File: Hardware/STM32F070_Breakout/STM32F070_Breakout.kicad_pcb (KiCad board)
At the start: 2 copper layers, 17.8 x 38.1 mm, 34 parts, among them J1 USB_B_Micro, J2 Conn_01x15, J3 Conn_01x15, J4 Conn_01x05, SW1 SW_Push, SW2 SW_Push, U1 AP2112K-3.3, U2 STM32F070CBT6, Y1 32.768kHZ, Y2 16MHz

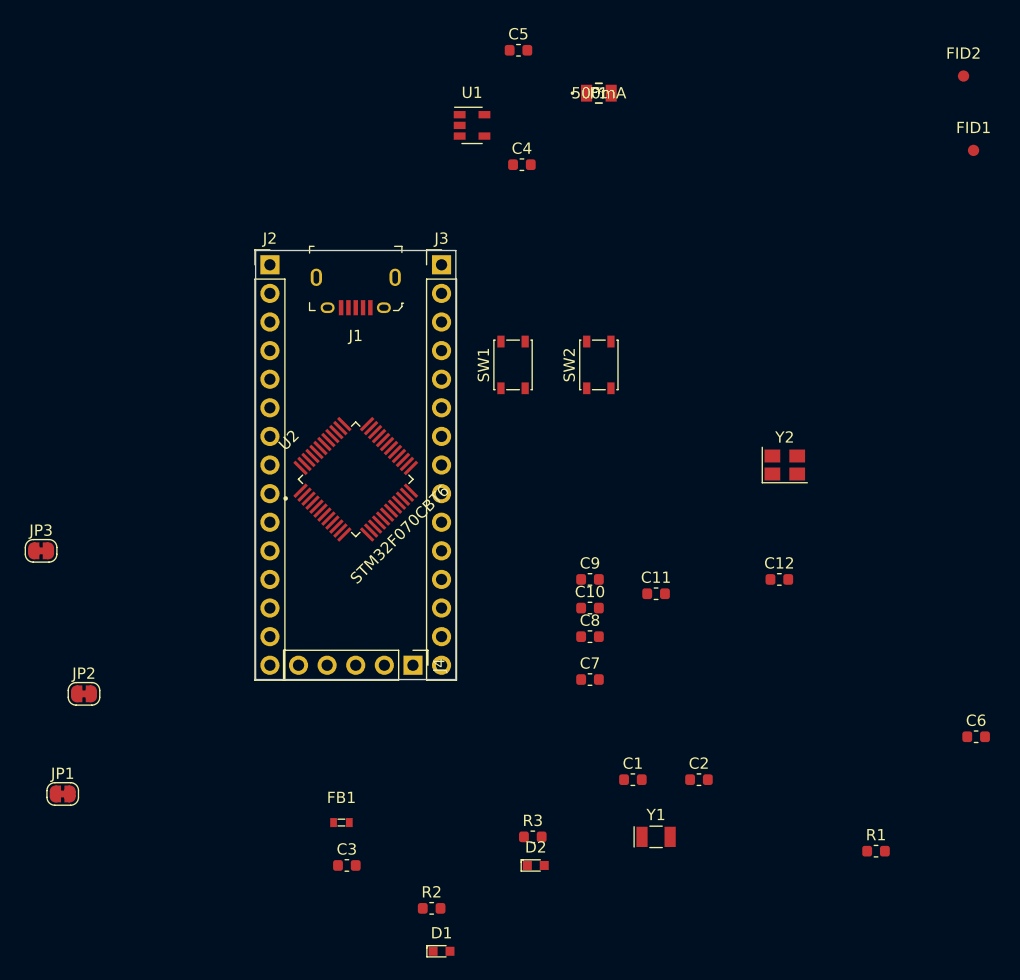
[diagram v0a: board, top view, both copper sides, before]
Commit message: Moved components around. Created BOM.
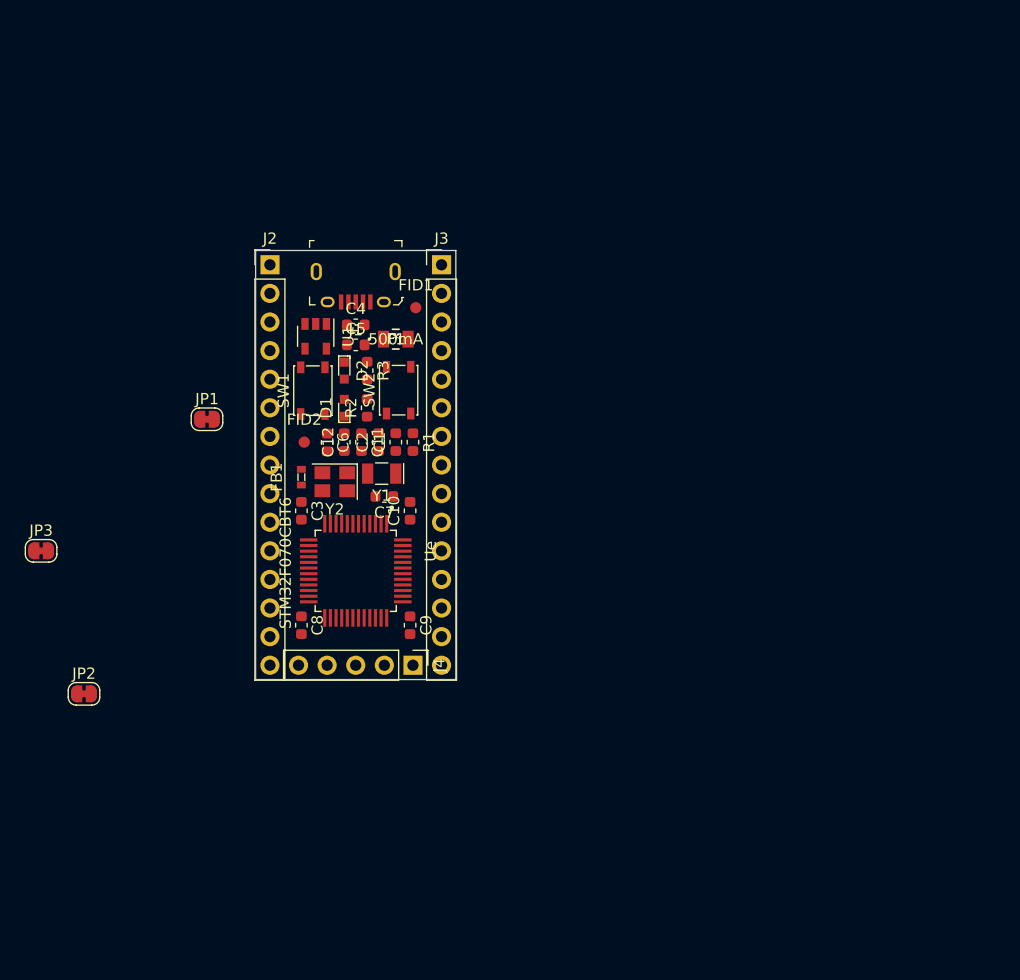
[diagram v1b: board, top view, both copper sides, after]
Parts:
- removed U2: STM32F070CBT6, STM32F070CBT6:QFP50P900X900X160-48N
- added Ue: STM32F070CBT6, STM32F070CBT6:QFP50P900X900X160-48N, F.Cu at (135.9, 104.6)
- moved FID2 67.0 mm to (131.3, 93.2)
- moved C6 63.3 mm to (133.3, 93.2), turned to 270 degrees
- moved R1 54.9 mm to (141.0, 93.2), turned to 270 degrees
- moved FID1 51.5 mm to (141.2, 81.3)
- moved D1 49.0 mm to (134.9, 90.2), turned to 90 degrees
- moved D2 47.1 mm to (134.9, 86.9), turned to 270 degrees
- moved R2 44.8 mm to (136.9, 90.2), turned to 90 degrees
- moved R3 43.9 mm to (136.9, 86.9), turned to 270 degrees
- moved C2 41.3 mm to (137.9, 93.2), turned to 90 degrees
- moved C12 40.5 mm to (134.9, 93.2), turned to 90 degrees
- moved Y1 40.4 mm to (138.2, 96.0), turned to 180 degrees
- moved Y2 40.0 mm to (134.0, 96.7), turned to 180 degrees
- moved C1 36.6 mm to (139.4, 93.2), turned to 90 degrees
- moved JP1 35.7 mm to (122.7, 91.2)
- moved C3 31.8 mm to (131.1, 99.3), turned to 270 degrees
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
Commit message: Components placed
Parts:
- removed Ue: STM32F070CBT6, STM32F070CBT6:QFP50P900X900X160-48N
- added U2: STM32F070CBT6, STM32F070CBT6:QFP50P900X900X160-48N, F.Cu at (135.9, 93.7)
- J2, J3: value Conn_01x15 -> Conn_01x16; footprint Connector_PinHeader_2.54mm:PinHeader_1x15_P2.54mm_Vertical -> Connector_PinHeader_2.54mm:PinHeader_1x16_P2.54mm_Vertical
- JP3: moved to B.Cu
- moved JP2 39.8 mm to (148.0, 98.9), turned to 270 degrees
- moved JP3 35.7 mm to (139.8, 86.9)
- moved JP1 31.4 mm to (149.7, 107.1), turned to 270 degrees
- moved SW2 23.2 mm to (132.1, 110.5)
- moved SW1 23.1 mm to (139.7, 110.5)
- moved C8 22.7 mm to (140.7, 88.9), turned to 90 degrees
- moved C9 22.7 mm to (131.1, 88.9), turned to 90 degrees
- moved D1 21.1 mm to (135.9, 111.3), turned to 0 degrees
- moved R2 19.6 mm to (135.9, 109.7), turned to 0 degrees
- moved R1 16.3 mm to (130.8, 105.9), turned to 90 degrees
- moved FID2 15.6 mm to (140.5, 105.9), turned to 180 degrees
- moved C1 14.6 mm to (132.3, 105.9), turned to 270 degrees
- moved C6 13.6 mm to (138.4, 105.9), turned to 90 degrees
- moved C2 13.3 mm to (133.9, 105.9), turned to 270 degrees
- moved C12 12.9 mm to (136.9, 105.9)
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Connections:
- J1 pad 2: USB_DM -> USB_D-
- J1 pad 3: USB_DP -> USB_D+
- J2 pad 1: AREF -> GND
- J2 pad 10: A6 -> D10
- J2 pad 11: A7 -> D11
- J2 pad 12: A8 -> D13
- J2 pad 13: A9 -> D14
- J2 pad 14: D0 -> D15
- J2 pad 15: D1 -> D16
- J2 pad 2: AGND -> D0
- J2 pad 3: RESET -> D1
- J2 pad 4: A0 -> D2
- J2 pad 5: A1 -> D3
- J2 pad 6: A2 -> D4
- J2 pad 7: A3 -> D5
- J2 pad 8: A4 -> D6
- J2 pad 9: A5 -> D7
- J3 pad 10: D7 -> A4
- J3 pad 11: D6 -> A3
- J3 pad 12: D5 -> A2
- J3 pad 13: D4 -> A1
- J3 pad 14: D3 -> A0
- J3 pad 15: D2 -> D17
- J3 pad 2: +3V3 -> GNDA
- J3 pad 3: GND -> +3V3
- J3 pad 4: D16 -> AREF
- J3 pad 5: D15 -> A9
- J3 pad 6: D14 -> A8
- J3 pad 7: D13 -> A7
- J3 pad 8: D11 -> A6
- J3 pad 9: D10 -> A5
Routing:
- net +3V3: track 0.00 -> 34.3 mm
- net D16: track 0.00 -> 27.8 mm, vias 0 -> 1
- net D15: track 0.00 -> 25.0 mm, vias 0 -> 1
- net D17: track 0.00 -> 24.0 mm, vias 0 -> 2
- net VIN: track 0.00 -> 23.5 mm, vias 0 -> 2
- net D14: track 0.00 -> 22.3 mm, vias 0 -> 1
- net D13: track 0.00 -> 19.5 mm, vias 0 -> 1
- net D11: track 0.00 -> 16.6 mm, vias 0 -> 1
- net D0: track 0.00 -> 15.5 mm, vias 0 -> 1
- net A0: track 0.00 -> 15.0 mm, vias 0 -> 1
- net D1: track 0.00 -> 14.9 mm, vias 0 -> 1
- net D10: track 0.00 -> 13.8 mm, vias 0 -> 1
- net RESET: track 0.00 -> 12.7 mm
- net A1: track 0.00 -> 12.3 mm, vias 0 -> 1
- net Net-(C12-Pad2): track 0.00 -> 10.1 mm
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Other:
- board size 17.8 x 38.1 mm -> 17.8 x 40.6 mm
- net class Default: clearance 0.254 -> 0.2032; trace_width 0.254 -> 0.2032; via_dia 0.762 -> 0.5588; via_drill 0.3556 -> 0.254
- net class Power added: clearance 0.2032, trace_width 0.3048, via_dia 0.5588, via_drill 0.254
- net class USB added: clearance 0.1524, trace_width 0.508, via_dia 0.5588, via_drill 0.254
- rule trace_clearance: 0.254 -> 0.2032
- rule trace_min: 0.000152 -> 0.1524
- rule via_min_drill: 0.000254 -> 0.0254
- rule via_min_size: 0.000508 -> 0.0508

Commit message: Layout done
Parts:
- J2, J3: footprint Connector_PinHeader_2.54mm:PinHeader_1x16_P2.54mm_Vertical -> STM32F070_Breakout:PinHeader_1x16_P2.54mm_Vertical_NoSilk
- J4: footprint Connector_PinHeader_2.54mm:PinHeader_1x05_P2.54mm_Vertical -> STM32F070_Breakout:PinHeader_1x05_P2.54mm_Vertical_NoSilk
- JP1, JP2: moved to B.Cu
- moved JP1 10.9 mm to (140.0, 102.2), turned to 90 degrees
- moved JP2 9.57 mm to (138.4, 98.0)
- moved JP3 1.51 mm to (138.3, 86.9)
- moved FID1 0.69 mm to (130.5, 81.2)
- moved FID2 0.38 mm to (140.5, 106.3)
- moved J4 0.25 mm to (130.8, 115.6)
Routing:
- net +3V3: track 34.3 -> 81.4 mm, vias 0 -> 4
- net SWDIO: track 0.00 -> 37.9 mm, vias 0 -> 1
- net SWCLK: track 0.00 -> 37.2 mm, vias 0 -> 1
- net GND: track 0.00 -> 35.1 mm, vias 0 -> 27
- net BOOT0: track 0.00 -> 26.1 mm, vias 0 -> 2
- net GNDA: track 0.00 -> 25.4 mm, vias 0 -> 2
- net AREF: track 6.13 -> 23.3 mm, vias 0 -> 1
- net RESET: track 12.7 -> 24.8 mm, vias 0 -> 2
- net Net-(FB1-Pad2): track 0.00 -> 4.07 mm, vias 0 -> 1
- net D0: track 15.5 -> 17.6 mm
- net A1: track 12.3 -> 13.8 mm
- net Net-(D2-Pad1): track 4.10 -> 2.89 mm
- net D14: track 22.3 -> 23.0 mm
- added copper zone on B.Cu, net GND
- added copper zone on F.Cu, net GND
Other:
- board text added: "0"
- board text added: "1"
- board text added: "10"
- board text added: "11"
- board text added: "13"
- board text added: "14"
- board text added: "15"
- board text added: "16"
- board text added: "17"
- board text added: "2"
- board text added: "3"
- board text added: "3V3"
- board text added: "4"
- board text added: "5"
- board text added: "6"
- board text added: "7"
- board text added: "A0"
- board text added: "A1"
- board text added: "A2"
- board text added: "A3"
- board text added: "A4"
- board text added: "A5"
- board text added: "A6"
- board text added: "A7"
- board text added: "A8"
- board text added: "A9"
- board text added: "AGND"
- board text added: "AREF"
- board text added: "BT0"
- board text added: "GND"
- board text added: "RST"
- board text added: "SWCLK"
- board text added: "SWDIO"
- board text added: "VIN"

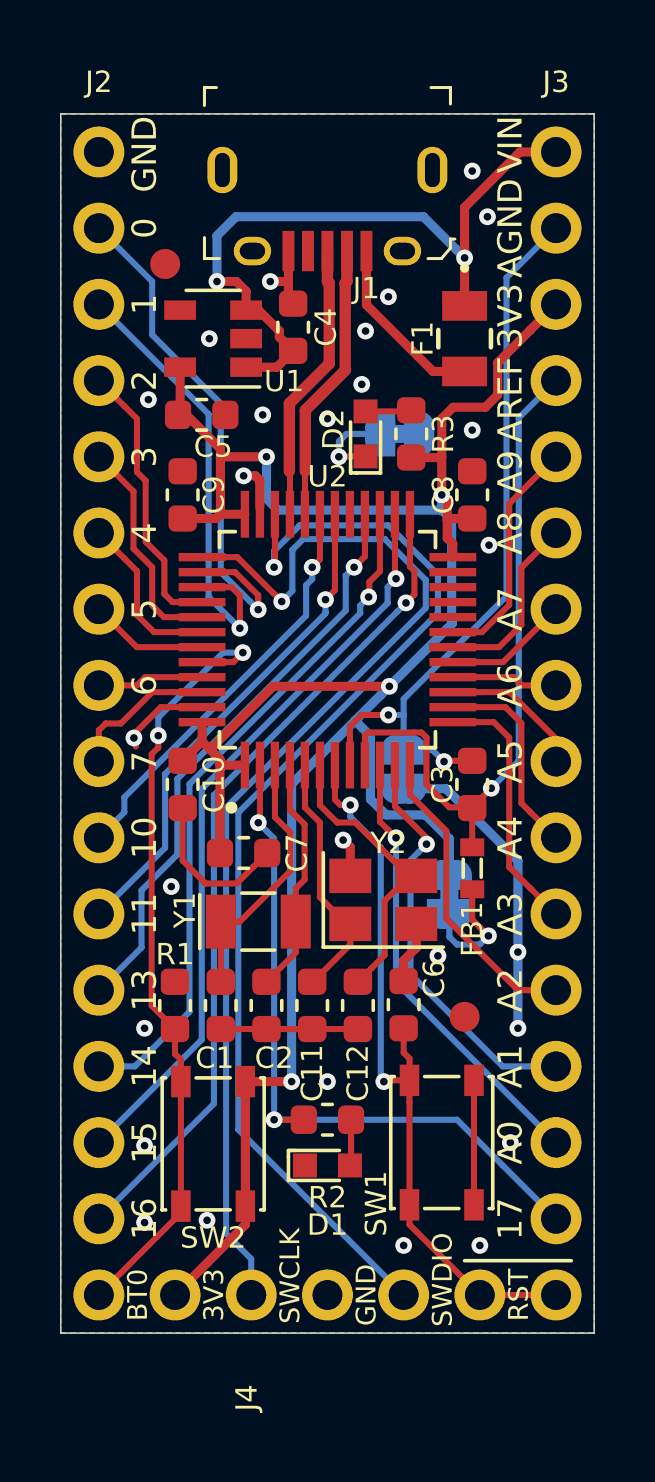
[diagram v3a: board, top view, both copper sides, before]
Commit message: Version v01 complete and sent for fab.
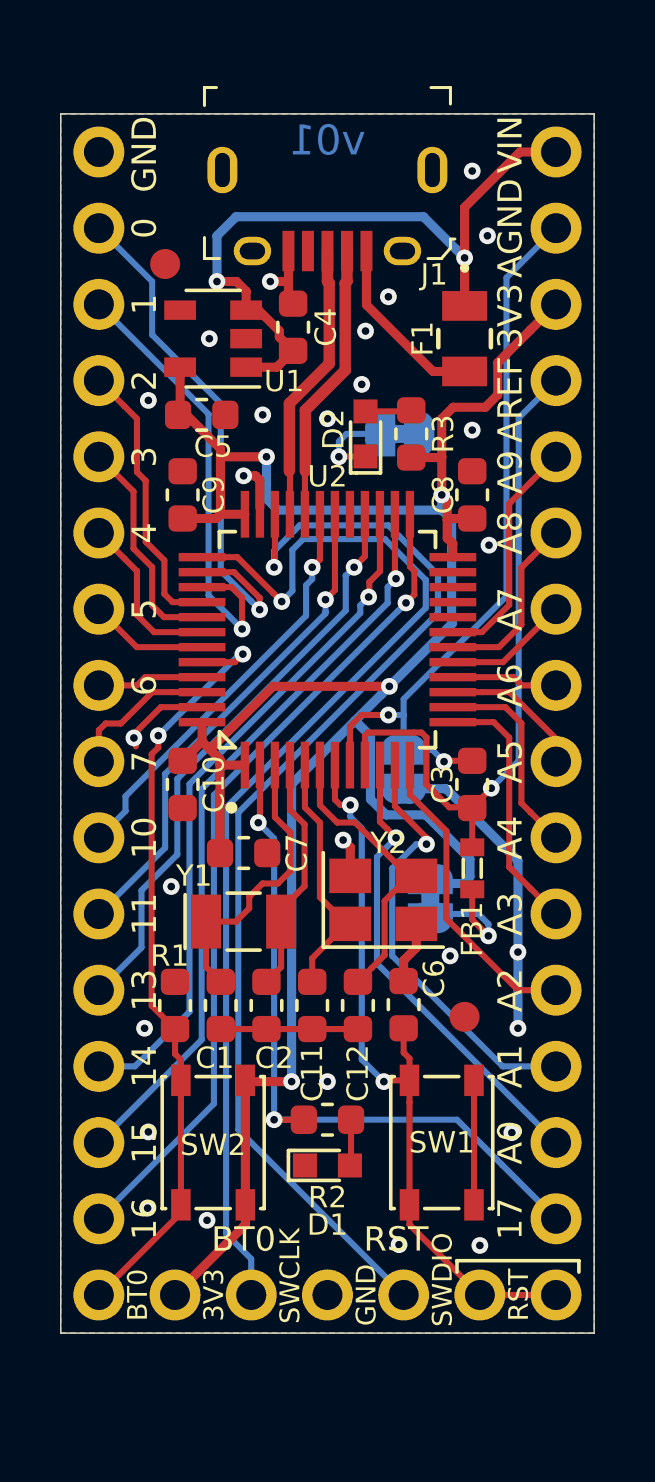
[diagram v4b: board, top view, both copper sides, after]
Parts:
- added G***: LOGO, STM32F070_Breakout:Shawn-Logo_5x5mm_SilkScreen, B.Cu at (135.9, 108.5)
- added G***: LOGO, STM32F070_Breakout:OSHW-Symbol_3.3x3mm_SilkScreen, B.Cu at (135.9, 94.4)
- J1: value USB_B_Micro -> 10118194-0001LF
- moved JP1 0.65 mm to (139.3, 102.4)
- moved Y1 0.49 mm to (133.1, 103.1)
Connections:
- J1 pad SH: (no net) -> GND
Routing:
- net GND: track 35.1 -> 29.8 mm
- net +3V3: track 81.4 -> 83.5 mm
- net Net-(C1-Pad1): track 8.77 -> 9.68 mm
- net A1: track 13.8 -> 14.5 mm
- net A0: track 15.0 -> 15.5 mm
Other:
- board text added: "3V3 AREF"
- board text added: "AGND GND"
- board text added: "PWR LED"
- board text added: "STM32F070 Breakout"
- board text added: "v01"

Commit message: Finished v02 layout
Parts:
- removed the G*** at (135.9, 108.5)
- added G***: LOGO, STM32F070_Breakout:Shawn-Logo_6x6mm_SilkScreen, B.Cu at (135.9, 108.3)
- added J5: Conn_01x01, STM32F070_Breakout:TestPoint_Pad_1.0x2.5mm, B.Cu at (138.2, 85.1)
- added J6: Conn_01x01, STM32F070_Breakout:TestPoint_Pad_1.0x2.5mm, B.Cu at (138.2, 83.7)
- added J7: Conn_01x01, STM32F070_Breakout:TestPoint_Pad_1.0x2.5mm, B.Cu at (138.2, 82.3)
- FB1: footprint digikey-footprints:0603 -> Resistor_SMD:R_0603_1608Metric
- R2, R3: value 330 -> 1k
- moved G*** 10.7 mm to (132.8, 84.1)
- moved JP3 0.40 mm to (138.2, 87.2)
- moved D2 0.38 mm to (137.2, 86.5)
- moved R3 0.38 mm to (138.7, 86.5)
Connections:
- net D17 renamed D20
- U2 pad 21: Net-(U2-Pad21) -> D30
- U2 pad 22: Net-(U2-Pad22) -> D31
- U2 pad 29: Net-(U2-Pad29) -> D12
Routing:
- net D30: track 0.00 -> 18.9 mm, vias 0 -> 1
- net D31: track 0.00 -> 13.3 mm, vias 0 -> 1
- net D12: track 0.00 -> 8.67 mm, vias 0 -> 1
- net GNDA: track 25.4 -> 27.2 mm
- net SWCLK: track 37.2 -> 36.0 mm
- net SWDIO: track 37.9 -> 36.9 mm
- net Net-(D2-Pad1): track 2.89 -> 2.15 mm
- net GND: vias 27 -> 24
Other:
- rule trace_min: 0.1524 -> 0
- board text added: "12"
- board text added: "20"
- board text added: "30"
- board text added: "31"
- board text added: "STM32F070CB"
- board text added: "YAS-0"
- board text added: "v02"
- board text removed: "17"
- board text removed: "STM32F070 Breakout"
- board text removed: "v01"

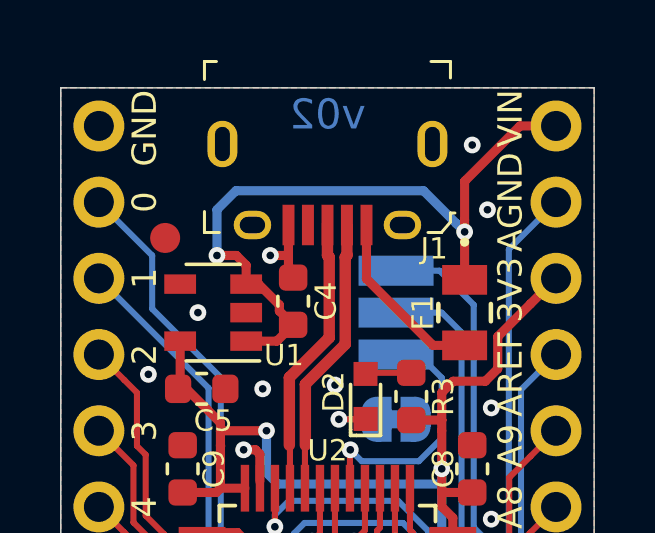
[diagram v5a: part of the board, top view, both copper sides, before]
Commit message: Added schematic pdf
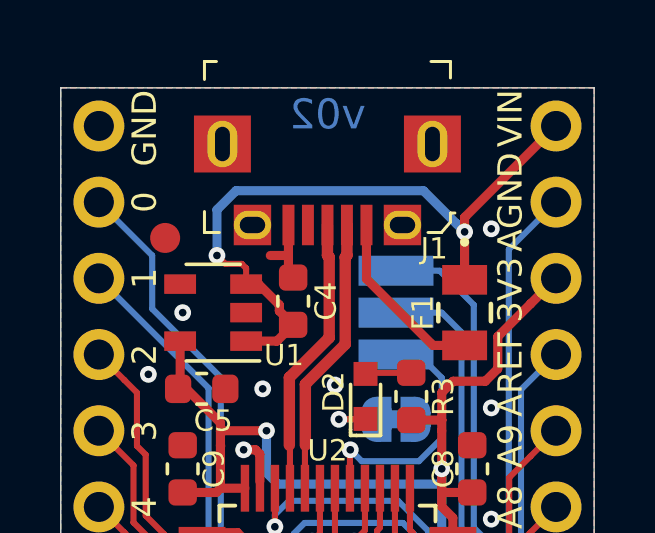
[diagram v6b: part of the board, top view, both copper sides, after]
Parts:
- J1: footprint digikey-footprints:USB_Micro_B_Female_10118194-0001LF -> STM32F070_Breakout:USB_Micro_B_Female_10118194-0001LF_oversized_pads
- moved G*** 0.13 mm to (132.7, 84.1)
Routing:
- net VIN: track 23.5 -> 22.7 mm
- net GND: vias 24 -> 22
